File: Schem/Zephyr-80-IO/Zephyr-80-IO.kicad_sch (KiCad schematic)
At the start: 0 parts

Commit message: Fixes to the IO Controller
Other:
- sheet Device Select Decode ports: added ~{RD}; removed none
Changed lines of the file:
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@@
 		(color 0 0 0 0)
 	)
+	(junction
+		(at 317.5 213.36)
+		(diameter 0)
+		(color 0 0 0 0)
+	)
 	(wire
 		(pts
@@
 	(wire
 		(pts
-			(xy 317.5 196.85) (xy 317.5 224.79)
+			(xy 317.5 196.85) (xy 317.5 213.36)
 		)
 		(stroke
@@
 	(wire
 		(pts
+			(xy 261.62 213.36) (xy 261.62 179.07)
+		)
+		(stroke
+			(width 0)
+			(type default)
+		)
+	)
+	(wire
+		(pts
 			(xy 292.1 251.46) (xy 256.54 251.46)
 		)
@@
 	(wire
 		(pts
+			(xy 317.5 213.36) (xy 261.62 213.36)
+		)
+		(stroke
+			(width 0)
+			(type default)
+		)
+	)
+	(wire
+		(pts
 			(xy 368.3 144.78) (xy 392.43 144.78)
 		)
@@
 		(pts
 			(xy 345.44 130.81) (xy 345.44 106.68)
+		)
+		(stroke
+			(width 0)
+			(type default)
+		)
+	)
+	(wire
+		(pts
+			(xy 317.5 213.36) (xy 317.5 224.79)
 		)
 		(stroke
@@
 			)
 		)
+		(pin "~{RD}" input
+			(at 261.62 179.07 270)
+			(effects
+				(font
+					(size 1.27 1.27)
+				)
+				(justify left)
+			)
+		)

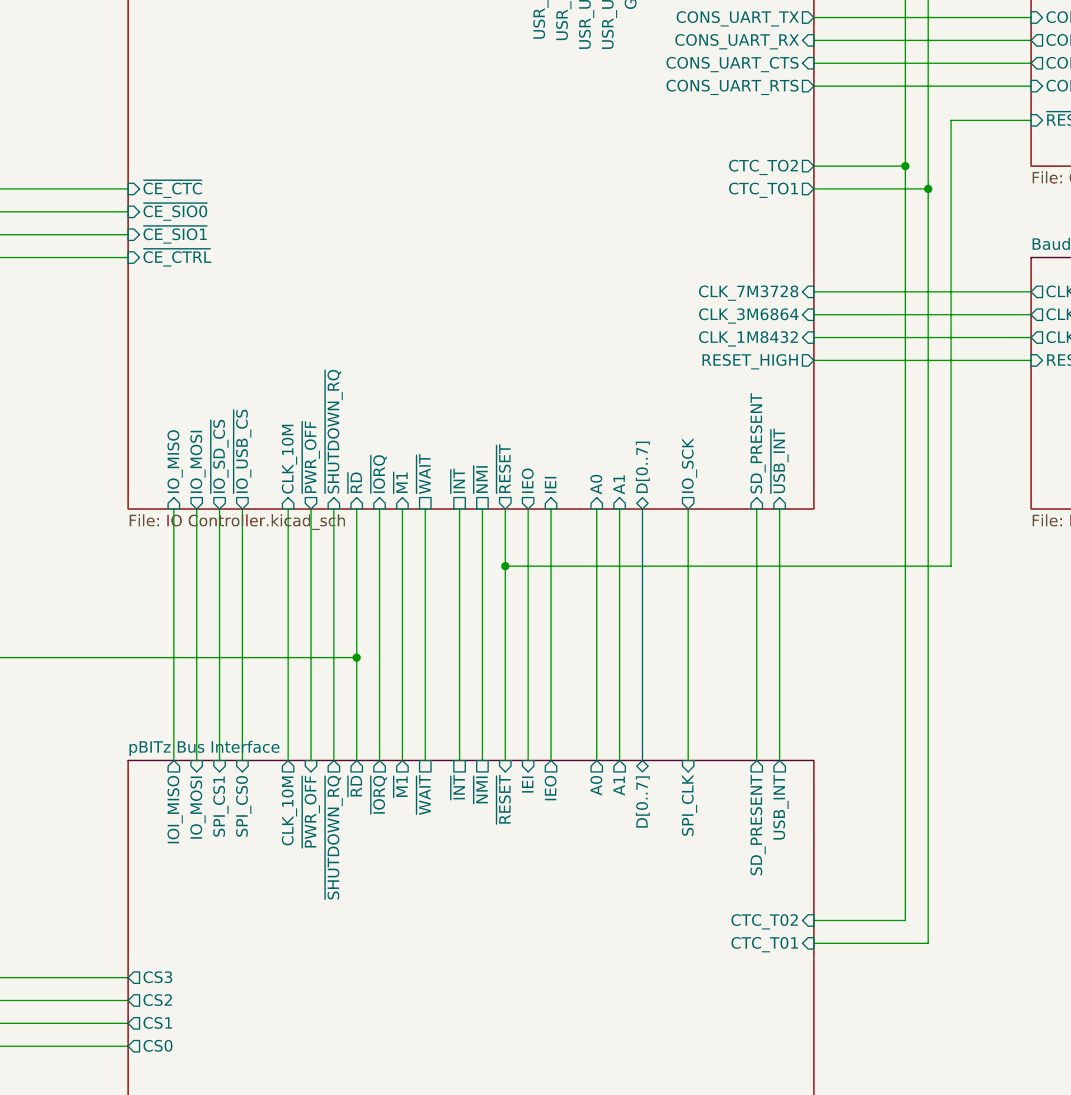
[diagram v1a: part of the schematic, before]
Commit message: Moved to the DIN Connector
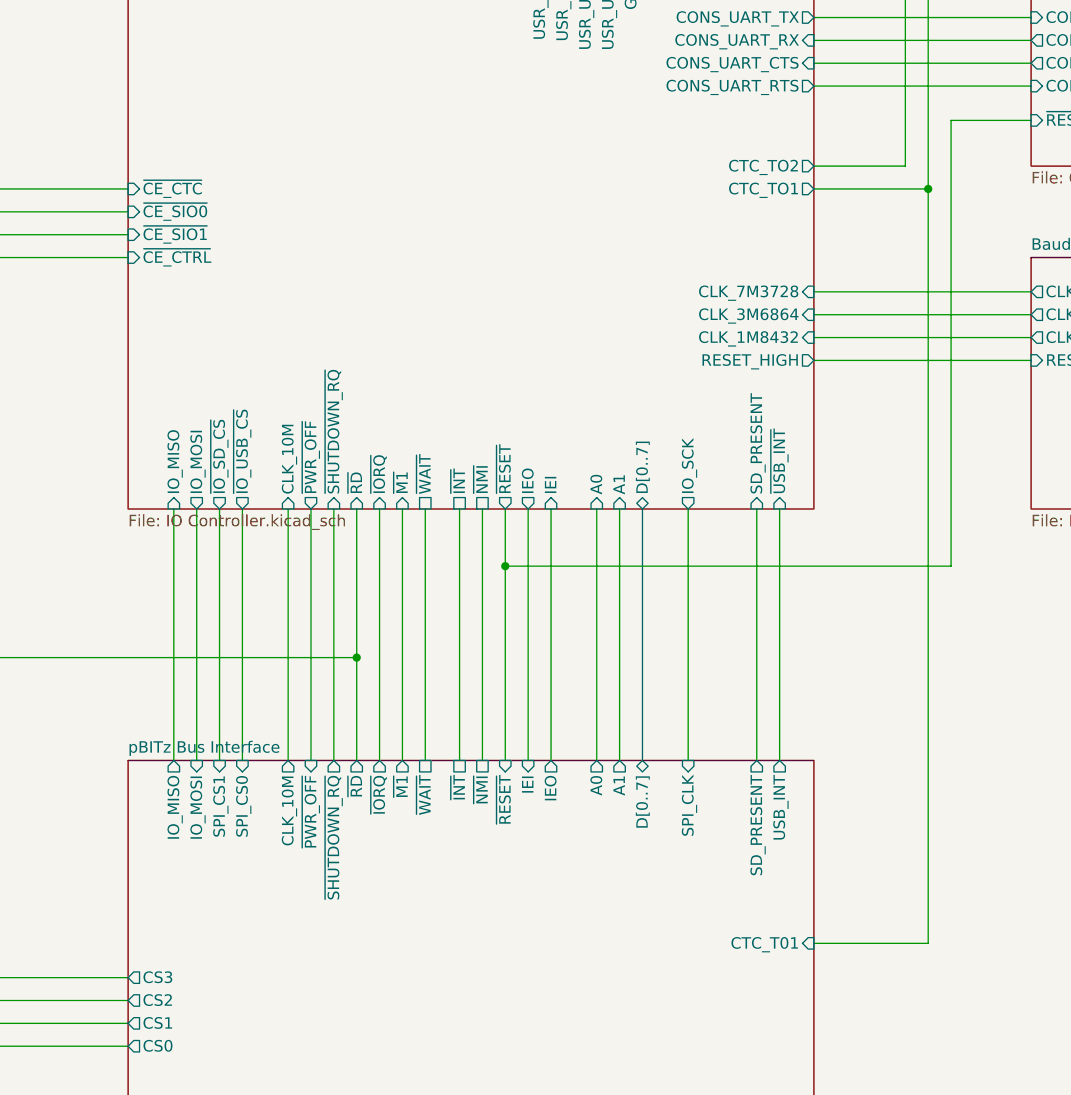
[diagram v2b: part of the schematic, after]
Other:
- sheet pBITz Bus Interface ports: added IO_MISO; removed CTC_T02, IOI_MISO
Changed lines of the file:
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@@
-	)
-	(junction
-		(at 378.46 158.75)
-		(diameter 0)
-		(color 0 0 0 0)
 	)
 	(junction
@@
 	(wire
 		(pts
-			(xy 378.46 158.75) (xy 378.46 242.57)
-		)
-		(stroke
-			(width 0)
-			(type default)
-		)
-	)
-	(wire
-		(pts
 			(xy 361.95 196.85) (xy 361.95 224.79)
 		)
@@
 		(pts
 			(xy 381 119.38) (xy 392.43 119.38)
-		)
-		(stroke
-			(width 0)
-			(type default)
-		)
-	)
-	(wire
-		(pts
-			(xy 378.46 242.57) (xy 368.3 242.57)
 		)
 		(stroke
@@
 			)
 		)
-		(pin "CTC_T02" input
-			(at 368.3 242.57 0)
-			(effects
-				(font
-					(size 1.27 1.27)
-				)
-				(justify right)
-			)
-		)
 		(pin "CS2" output
 			(at 292.1 251.46 180)
@@
 			)
 		)
-		(pin "IOI_MISO" output
+		(pin "IO_MISO" output
 			(at 297.18 224.79 90)
 			(effects
